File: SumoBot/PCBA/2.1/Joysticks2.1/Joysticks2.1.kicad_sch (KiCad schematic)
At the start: 21 parts, among them J1 Screw_Terminal_01x02, J4 OLED SCREEN, U1 THB001P, U11 THB001P, U2 MX1A-11NN, U3 MX1A-11NN, U4 MX1A-11NN, U5 MX1A-11NN, U6 NRF24L01_Breakout

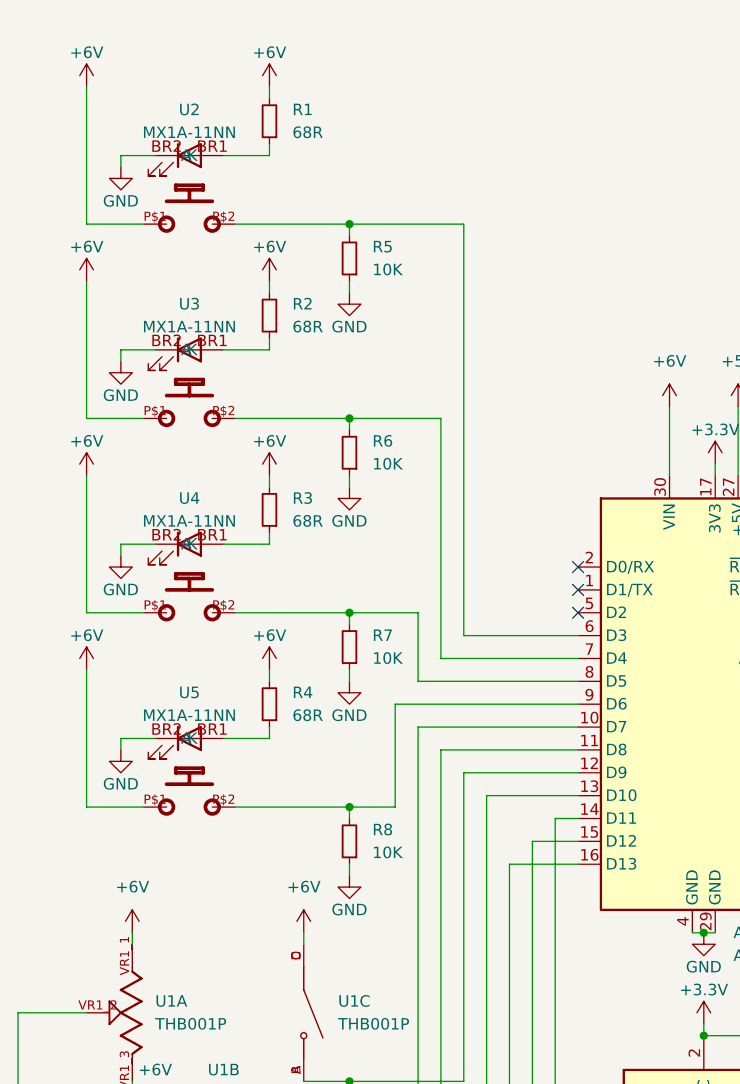
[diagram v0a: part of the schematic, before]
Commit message: added notes to sumonyx pcbs
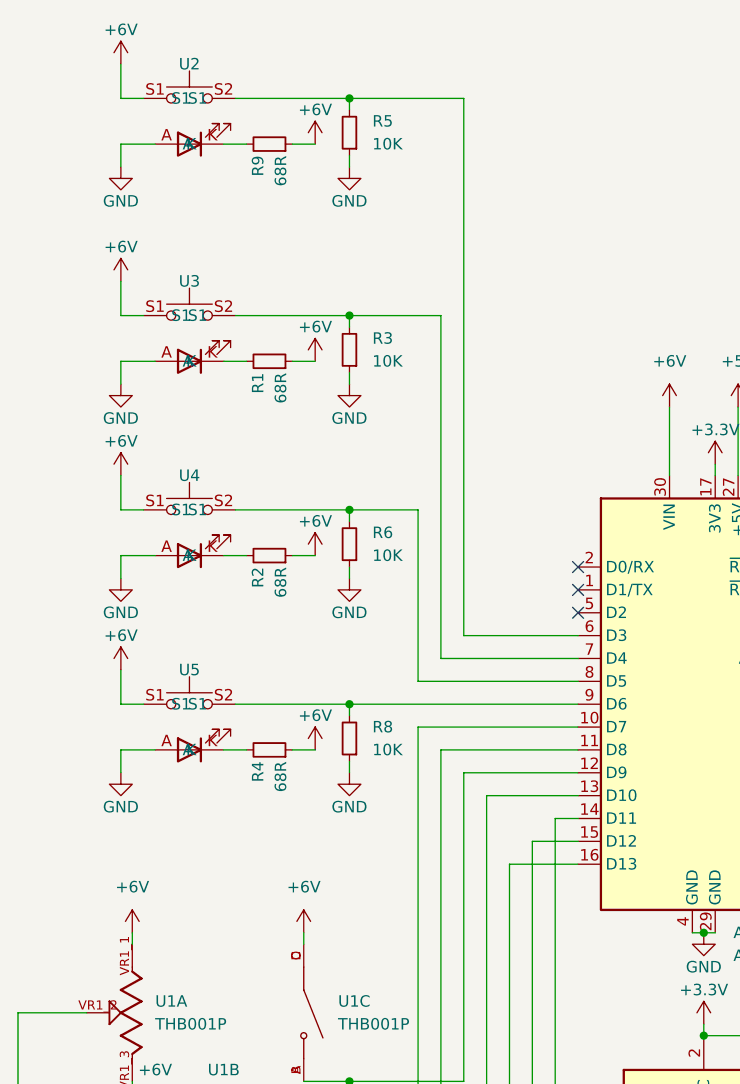
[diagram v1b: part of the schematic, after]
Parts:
- removed R7: 10K, Resistor_SMD:R_0805_2012Metric, symbol Device:R_Small
- removed U2, U3, U4, U5: MX1A-11NN, MX1A-11NN:CHERRY_MX1A-11NN_SWITCH, symbol MX1A-11NN:MX1A-11NN
- added R9: 68R, Resistor_SMD:R_0805_2012Metric, symbol Device:R_Small
- added U2, U3, U4, U5: ~, Button_Switch_Keyboard:SW_Cherry_MX_3mmLED, symbol Switch:CherryMX_LED
- R3: value 68R -> 10K
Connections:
- net +6V: now also R1.1, R2.1, R4.1, R9.1, U2.S1, U3.S1, U4.S1, U5.S1; no longer R1.2, R2.2, R3.2, R4.2
- net GND: now also R3.1, U2.A, U3.A, U4.A, U5.A
- net at A1.6 (D3), R5.2: now also U2.S2 (S1)
- net at R6.2: now also A1.8 (D5), U4.S2 (S1); no longer A1.7 (D4)
- net at A1.9 (D6), R8.2: now also U5.S2 (S1)
- new net: R2.2, U4.K
- new net: R1.2, U3.K
- new net: A1.7 (D4), R3.2, U3.S2 (S1)
- new net: R4.2, U5.K
- new net: R9.2, U2.K
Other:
- moved on the sheet: R5
